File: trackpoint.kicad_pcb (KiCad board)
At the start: 2 copper layers, 27.5 x 35 mm, 28 parts, among them P1 CONN_10, P2 CONN_5, P3 CONN_8, U1 MKL03Z32VFK4, U4 ESD

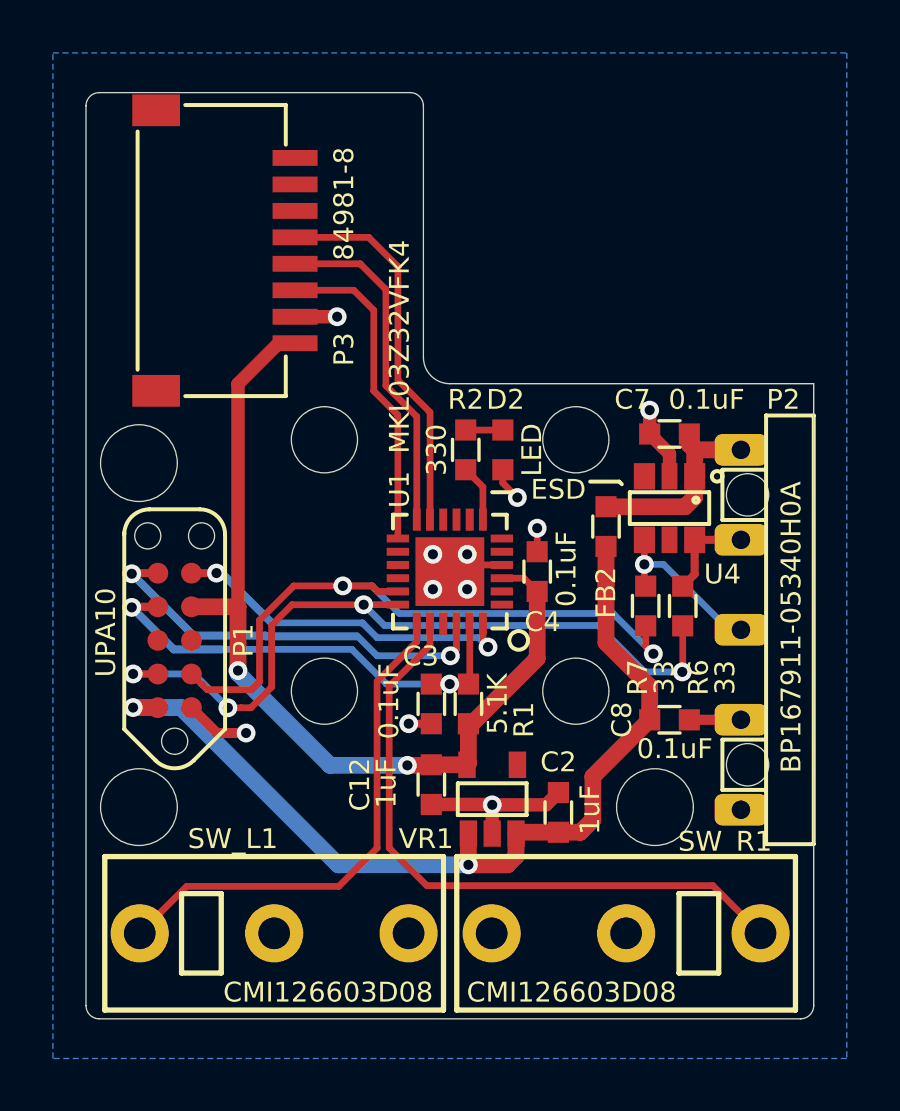
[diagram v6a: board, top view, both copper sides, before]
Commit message: Update PCB based on CAD.
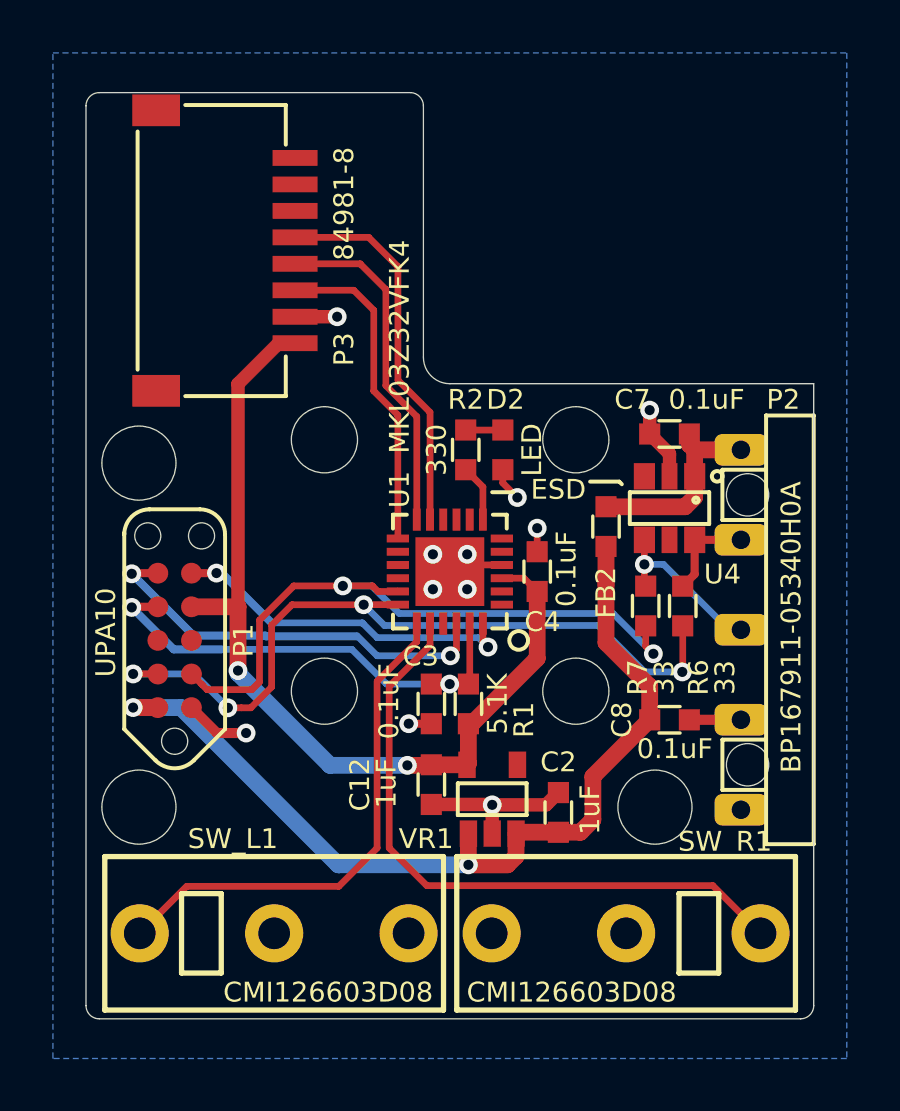
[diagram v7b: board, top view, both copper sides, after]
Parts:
- removed the ? at (194.2, 126.5)
- removed the ? at (213.8, 139.5)
- removed the ? at (194.2, 139.5)
- added ?: , ugl:hole_2.8mm, F.Cu at (194.2, 126.5)
- added ?: , ugl:hole_2.8mm, F.Cu at (213.8, 139.5)
- added ?: , ugl:hole_2.8mm, F.Cu at (194.2, 139.5)
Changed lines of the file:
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@@
   (general
     (thickness 1.6)
-    (drawings 24)
+    (drawings 44)
     (tracks 212)
     (zones 0)
@@
     (41 Cmts.User user)
     (42 Eco1.User user)
-    (43 Eco2.User user)
+    (43 Eco2.User user hide)
     (44 Edge.Cuts user)
     (45 Margin user)
@@
   )
   (setup
-    (last_trace_width 0.381)
+    (last_trace_width 0.254)
     (user_trace_width 0.254)
     (user_trace_width 0.3048)
@@
     (add_net "Net-(VR1-Pad4)")
   )
+  (module ugl:hole_2.8mm locked (layer F.Cu)
+    (at 194.25 126.5)
+    (attr virtual)
+    (fp_text reference "" (at 0 0) (layer F.SilkS)
+      (effects (font (size 1.27 1.27) (thickness 0.15)))
+    )
+    (fp_text value "" (at 0 0) (layer F.SilkS)
+      (effects (font (size 1.27 1.27) (thickness 0.15)))
+    )
+    (pad "" np_thru_hole circle (at 0 0) (size 2.8 2.8) (drill 2.8) (layers *.Cu *.Mask))
+  )
+  (module ugl:hole_2.8mm locked (layer F.Cu)
+    (at 213.75 139.5)
+    (attr virtual)
+    (fp_text reference "" (at 0 0) (layer F.SilkS)
+      (effects (font (size 1.27 1.27) (thickness 0.15)))
+    )
+    (fp_text value "" (at 0 0) (layer F.SilkS)
+      (effects (font (size 1.27 1.27) (thickness 0.15)))
+    )
+    (pad "" np_thru_hole circle (at 0 0) (size 2.8 2.8) (drill 2.8) (layers *.Cu *.Mask))
+  )
+  (module ugl:hole_2.8mm locked (layer F.Cu)
+    (at 194.25 139.5)
+    (attr virtual)
+    (fp_text reference "" (at 0 0) (layer F.SilkS)
+      (effects (font (size 1.27 1.27) (thickness 0.15)))
+    )
+    (fp_text value "" (at 0 0) (layer F.SilkS)
+      (effects (font (size 1.27 1.27) (thickness 0.15)))
+    )
+    (pad "" np_thru_hole circle (at 0 0) (size 2.8 2.8) (drill 2.8) (layers *.Cu *.Mask))
+  )
   (module ugl:CMI126603D08 locked (layer F.Cu)
     (at 212.660004 144.268997 180)
@@
       (rotate (xyz 0 0 0))
     )
-  )
-  (module ugl:hole_2.9mm locked (layer F.Cu)
-    (at 194.25 126.5)
-    (solder_mask_margin 0.2)
-    (clearance 0.2)
-    (attr virtual)
-    (fp_text reference "" (at 0 0) (layer F.SilkS)
-      (effects (font (size 1.27 1.27) (thickness 0.15)))
-    )
-    (fp_text value "" (at 0 0) (layer F.SilkS)
-      (effects (font (size 1.27 1.27) (thickness 0.15)))
-    )
-    (pad "" np_thru_hole circle (at 0 0) (size 2.9 2.9) (drill 2.9) (layers *.Cu *.Mask))
-  )
-  (module ugl:hole_2.9mm locked (layer F.Cu)
-    (at 213.75 139.5)
-    (solder_mask_margin 0.2)
-    (clearance 0.2)
-    (attr virtual)
-    (fp_text reference "" (at 0 0) (layer F.SilkS)
-      (effects (font (size 1.27 1.27) (thickness 0.15)))
-    )
-    (fp_text value "" (at 0 0) (layer F.SilkS)
-      (effects (font (size 1.27 1.27) (thickness 0.15)))
-    )
-    (pad "" np_thru_hole circle (at 0 0) (size 2.9 2.9) (drill 2.9) (layers *.Cu *.Mask))
-  )
-  (module ugl:hole_2.9mm locked (layer F.Cu)
-    (at 194.25 139.5)
-    (solder_mask_margin 0.2)
-    (clearance 0.2)
-    (attr virtual)
-    (fp_text reference "" (at 0 0) (layer F.SilkS)
-      (effects (font (size 1.27 1.27) (thickness 0.15)))
-    )
-    (fp_text value "" (at 0 0) (layer F.SilkS)
-      (effects (font (size 1.27 1.27) (thickness 0.15)))
-    )
-    (pad "" np_thru_hole circle (at 0 0) (size 2.9 2.9) (drill 2.9) (layers *.Cu *.Mask))
   )
   (module ugl:Tag_Connect_2x5_Header_With_No_Legs_Parallel_Numbering (layer F.Cu)
@@
   (gr_line (start 212.4 127.2) (end 212.5 127.3) (layer F.SilkS) (width 0.15))
   (gr_line (start 211.3 127.2) (end 212.4 127.2) (layer F.SilkS) (width 0.15))
-  (gr_circle (center 210.760002 125.619003) (end 212.660002 125.619003) (layer Eco1.User) (width 0.01))
-  (gr_circle (center 210.760002 135.119003) (end 212.660002 135.119003) (layer Eco1.User) (width 0.01))
-  (gr_circle (center 201.260002 135.119003) (end 203.160002 135.119003) (layer Eco1.User) (width 0.01))
-  (gr_circle (center 201.260002 125.619003) (end 203.160002 125.619003) (layer Eco1.User) (width 0.01))
-  (gr_line (start 204.5 112.5) (end 192.75 112.5) (angle 90) (layer Edge.Cuts) (width 0.01))
-  (gr_line (start 192.25 113) (end 192.25 147) (angle 90) (layer Edge.Cuts) (width 0.01))
-  (gr_line (start 219.75 123.5) (end 206 123.5) (angle 90) (layer Edge.Cuts) (width 0.01))
   (gr_text "PCB ID: trackpoint_main_1.0.0" (at 206.1 146.5) (layer B.SilkS)
     (effects (font (size 0.75 0.75) (thickness 0.15)) (justify mirror))
   )
-  (gr_arc (start 192.75 146.999993) (end 192.25 147) (angle -89.99010657) (layer Edge.Cuts) (width 0.01))
+  (gr_circle (center 194.25 139.5) (end 196 139.5) (layer Eco1.User) (width 0.01))
+  (gr_circle (center 213.75 139.5) (end 215.5 139.5) (layer Eco1.User) (width 0.01))
+  (gr_circle (center 194.25 126.5) (end 196 126.5) (layer Eco1.User) (width 0.01))
+  (gr_line (start 210.32501 127.048678) (end 210.32501 126.791542) (angle 90) (layer Eco1.User) (width 0.01))
+  (gr_line (start 209.330992 125.01395) (end 209.666563 125.01395) (angle 90) (layer Eco1.User) (width 0.01))
+  (gr_line (start 209.031037 126.049515) (end 209.031037 125.313905) (angle 90) (layer Eco1.User) (width 0.01))
+  (gr_line (start 209.588128 126.05466) (end 209.330992 126.05466) (angle 90) (layer Eco1.User) (width 0.01))
+  (gr_line (start 211.065765 127.348633) (end 210.330155 127.348633) (angle 90) (layer Eco1.User) (width 0.01))
+  (gr_line (start 211.36572 126.713107) (end 211.36572 127.048678) (angle 90) (layer Eco1.User) (width 0.01))
+  (gr_line (start 202.689008 126.05466) (end 202.431872 126.05466) (angle 90) (layer Eco1.User) (width 0.01))
+  (gr_line (start 200.65428 127.048678) (end 200.65428 126.713107) (angle 90) (layer Eco1.User) (width 0.01))
+  (gr_line (start 201.689845 127.348633) (end 200.954235 127.348633) (angle 90) (layer Eco1.User) (width 0.01))
+  (gr_line (start 201.69499 126.791542) (end 201.69499 127.048678) (angle 90) (layer Eco1.User) (width 0.01))
+  (gr_line (start 202.988963 125.313905) (end 202.988963 126.049515) (angle 90) (layer Eco1.User) (width 0.01))
+  (gr_line (start 202.353437 125.01395) (end 202.689008 125.01395) (angle 90) (layer Eco1.User) (width 0.01))
+  (gr_line (start 201.69499 133.690662) (end 201.69499 133.947798) (angle 90) (layer Eco1.User) (width 0.01))
+  (gr_line (start 202.689008 135.72539) (end 202.353437 135.72539) (angle 90) (layer Eco1.User) (width 0.01))
+  (gr_line (start 202.988963 134.689825) (end 202.988963 135.425436) (angle 90) (layer Eco1.User) (width 0.01))
+  (gr_line (start 202.431872 134.68468) (end 202.689008 134.68468) (angle 90) (layer Eco1.User) (width 0.01))
+  (gr_line (start 200.954235 133.390708) (end 201.689845 133.390708) (angle 90) (layer Eco1.User) (width 0.01))
+  (gr_line (start 200.65428 134.026234) (end 200.65428 133.690662) (angle 90) (layer Eco1.User) (width 0.01))
+  (gr_line (start 209.330992 134.68468) (end 209.588128 134.68468) (angle 90) (layer Eco1.User) (width 0.01))
+  (gr_line (start 211.36572 133.690662) (end 211.36572 134.026234) (angle 90) (layer Eco1.User) (width 0.01))
+  (gr_line (start 210.330155 133.390708) (end 211.065765 133.390708) (angle 90) (layer Eco1.User) (width 0.01))
+  (gr_line (start 210.32501 133.947798) (end 210.32501 133.690662) (angle 90) (layer Eco1.User) (width 0.01))
+  (gr_line (start 209.031037 135.425436) (end 209.031037 134.689825) (angle 90) (layer Eco1.User) (width 0.01))
+  (gr_line (start 209.666563 135.72539) (end 209.330992 135.72539) (angle 90) (layer Eco1.User) (width 0.01))
+  (gr_arc (start 205.999992 122.500001) (end 205 122.5) (angle -89.99818777) (layer Edge.Cuts) (width 0.01))
+  (gr_line (start 205 113) (end 205 122.5) (angle 90) (layer Edge.Cuts) (width 0.01))
+  (gr_line (start 192.75 112.5) (end 204.5 112.5) (angle 90) (layer Edge.Cuts) (width 0.01))
+  (gr_arc (start 204.5 113.000007) (end 205 113) (angle -89.99010657) (layer Edge.Cuts) (width 0.01))
   (gr_arc (start 219.25 146.999993) (end 219.25 147.5) (angle -90.00451968) (layer Edge.Cuts) (width 0.01))
+  (gr_arc (start 192.750003 146.999993) (end 192.25 147) (angle -89.99221755) (layer Edge.Cuts) (width 0.01))
+  (gr_arc (start 192.750003 113.000007) (end 192.75 112.5) (angle -89.99942428) (layer Edge.Cuts) (width 0.01))
+  (gr_line (start 219.75 123.5) (end 206 123.5) (angle 90) (layer Edge.Cuts) (width 0.01))
+  (gr_line (start 219.75 147) (end 219.75 123.5) (angle 90) (layer Edge.Cuts) (width 0.01))
   (gr_line (start 192.75 147.5) (end 219.25 147.5) (angle 90) (layer Edge.Cuts) (width 0.01))
-  (gr_circle (center 194.25 139.5) (end 195.9 139.5) (layer Eco1.User) (width 0.01))
-  (gr_circle (center 213.75 139.5) (end 215.4 139.5) (layer Eco1.User) (width 0.01))
-  (gr_circle (center 194.25 126.5) (end 195.9 126.5) (layer Eco1.User) (width 0.01))
-  (gr_arc (start 205.999992 122.500001) (end 205 122.5) (angle -90) (layer Edge.Cuts) (width 0.01))
-  (gr_line (start 205 122.5) (end 205 113) (angle 90) (layer Edge.Cuts) (width 0.01))
-  (gr_arc (start 204.500007 113) (end 205.000007 112.999993) (angle -90) (layer Edge.Cuts) (width 0.01))
-  (gr_arc (start 192.75 113.000007) (end 192.75 112.5) (angle -90) (layer Edge.Cuts) (width 0.01))
-  (gr_line (start 219.75 147) (end 219.75 123.5) (angle 90) (layer Edge.Cuts) (width 0.01))
+  (gr_line (start 192.25 147) (end 192.25 113) (angle 90) (layer Edge.Cuts) (width 0.01))
   (segment (start 215.25 126.000003) (end 215.25 127) (width 0.635) (layer F.Cu) (net 1))
   (segment (start 217 126.000003) (end 215.25 126.000003) (width 0.635) (layer F.Cu) (net 1))

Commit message: Bump version to 1.1.0
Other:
- board text added: "PCB ID: trackpoint_main_1.1.0"
- board text removed: "PCB ID: trackpoint_main_1.0.0"
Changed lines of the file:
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@@
   (title_block
     (title "UHK Trackpoint Module")
-    (rev 1.0.0)
+    (rev 1.1.0)
     (company "Ultimate Gadget Laboratories Kft.")
   )
@@
   (gr_line (start 212.4 127.2) (end 212.5 127.3) (layer F.SilkS) (width 0.15))
   (gr_line (start 211.3 127.2) (end 212.4 127.2) (layer F.SilkS) (width 0.15))
-  (gr_text "PCB ID: trackpoint_main_1.0.0" (at 206.1 146.5) (layer B.SilkS)
+  (gr_text "PCB ID: trackpoint_main_1.1.0" (at 206.1 146.5) (layer B.SilkS)
     (effects (font (size 0.75 0.75) (thickness 0.15)) (justify mirror))
   )
